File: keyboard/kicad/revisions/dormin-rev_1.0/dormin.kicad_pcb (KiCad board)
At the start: 2 copper layers, 141.5 x 103.1 mm, 108 parts, among them J1 Conn_01x06, J2 Conn_01x04, J3 Conn_01x05, Q1 HX2302A, SW1 SW_Push, SW10 SW_Push, SW11 SW_Push, SW12 SW_Push, SW13 SW_Push, SW14 SW_Push, SW15 SW_Push, SW16 SW_Push, SW17 SW_Push, SW18 SW_Push, SW19 SW_Push, SW2 SW_Push, SW20 SW_Push, SW3 SW_Push, SW4 SW_Push, SW5 SW_Push, SW6 SW_Push, SW7 SW_Push, SW8 SW_Push, SW9 SW_Push, U3 XIAO-nRF52840-Plus-SMD, U4 TPD2E2U06DCK

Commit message: feat: improve schematics and pcb components placements
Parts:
- added C3: 10uF, Capacitor_SMD:C_0603_1608Metric, B.Cu at (74.1, 96.2)
- added C4: 100nF, Capacitor_SMD:C_0603_1608Metric, B.Cu at (68.4, 96.1)
- added Q2: AO3407A, Package_TO_SOT_SMD:SOT-23, B.Cu at (199.9, 124.0)
- added R710: 100R, Resistor_SMD:R_0603_1608Metric, B.Cu at (199.7, 119.4)
- added R711: 100k, Resistor_SMD:R_0603_1608Metric, B.Cu at (201.4, 119.4)
- added R712: 330R, Resistor_SMD:R_0603_1608Metric, B.Cu at (197.9, 119.4)
- D27: footprint Diode_SMD:Nexperia_CFP3_SOD-123W -> Diode_SMD:D_SOD-523
- D28: value SMF5V0A -> KPESD5V0S1UL; footprint Diode_SMD:D_SMF -> Diode_SMD:D_SOD-882
- J3: value Conn_01x05 -> Conn_01x04
- JST1: footprint willkeebs_power:JST_1.25mm -> Connector_JST:JST_GH_SM02B-GHS-TB_1x02-1MP_P1.25mm_Horizontal
- PSW1: footprint willkeebs_power:Switch_MSK12C02 -> PCM_marbastlib-various:SW_MSK12C02-HB
- Q1: value HX2302A -> AO3400A
- R23, R5, R6: footprint Resistor_SMD:R_0402_1005Metric -> Resistor_SMD:R_0603_1608Metric
- RSW1: footprint willkeebs_components:SW_Push_1P1T_XKB_TS-1187A -> Button_Switch_SMD:SW_SPST_SKQG_WithStem
- moved C2 20.5 mm to (181.2, 103.7), turned to 90 degrees
- moved C1 20.5 mm to (179.4, 103.7), turned to 90 degrees
- moved F2 18.6 mm to (197.5, 133.4), turned to 0 degrees
- moved D27 15.5 mm to (198.5, 131.3), turned to 0 degrees
- moved R1 15.3 mm to (164.2, 103.7), turned to 90 degrees
- moved R6 13.5 mm to (186.1, 119.4)
- moved R5 13.2 mm to (187.9, 119.4)
- moved R23 13.0 mm to (189.6, 119.4)
- moved D11 4.92 mm to (68.5, 114.1), turned to -90 degrees
- moved R706 3.70 mm to (188.9, 128.8)
- moved Q1 3.70 mm to (185.4, 131.0)
- moved R707 3.70 mm to (188.9, 133.3)
- moved D28 1.74 mm to (198.8, 129.6), turned to 0 degrees
- moved U4 0.57 mm to (198.1, 136.1)
- turned D14 to 180 degrees
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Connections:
- net LED_SWITCH renamed BL_DRAIN
- D21 pad 2: RGB_DATA -> Net-(D21-DIN)
- D21 pad 3: 3V3 -> EXT_VCC
- D22 pad 3: 3V3 -> EXT_VCC
- D23 pad 3: 3V3 -> EXT_VCC
- D24 pad 3: 3V3 -> EXT_VCC
- U3 pad 17: RGB_DATA -> STS_LED_DATA
- U3 pad 19: unconnected-(U3-D15_NFC2-Pad19) -> POWER_PIN
- U3 pad 21: EXTB -> EXTA
- U3 pad 22: EXTA -> EXTB
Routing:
- net 5V: track 0.00 -> 40.2 mm
- net VBAT: track 0.00 -> 26.7 mm
- net EXT_VCC: track 0.00 -> 23.2 mm
- net Net-(D22-DOUT): track 0.00 -> 17.2 mm, vias 0 -> 2
- net Net-(D23-DOUT): track 0.00 -> 15.8 mm, vias 0 -> 2
- net Net-(D21-DOUT): track 0.00 -> 15.7 mm
- net GND: track 0.00 -> 11.1 mm, vias 0 -> 4
- net Net-(J3-Pin_3): track 0.00 -> 9.55 mm, vias 0 -> 2
- net Net-(J3-Pin_4): track 0.00 -> 9.44 mm, vias 0 -> 2
- net Net-(D27-K): track 0.00 -> 9.11 mm
- net Net-(D27-A): track 0.00 -> 2.24 mm

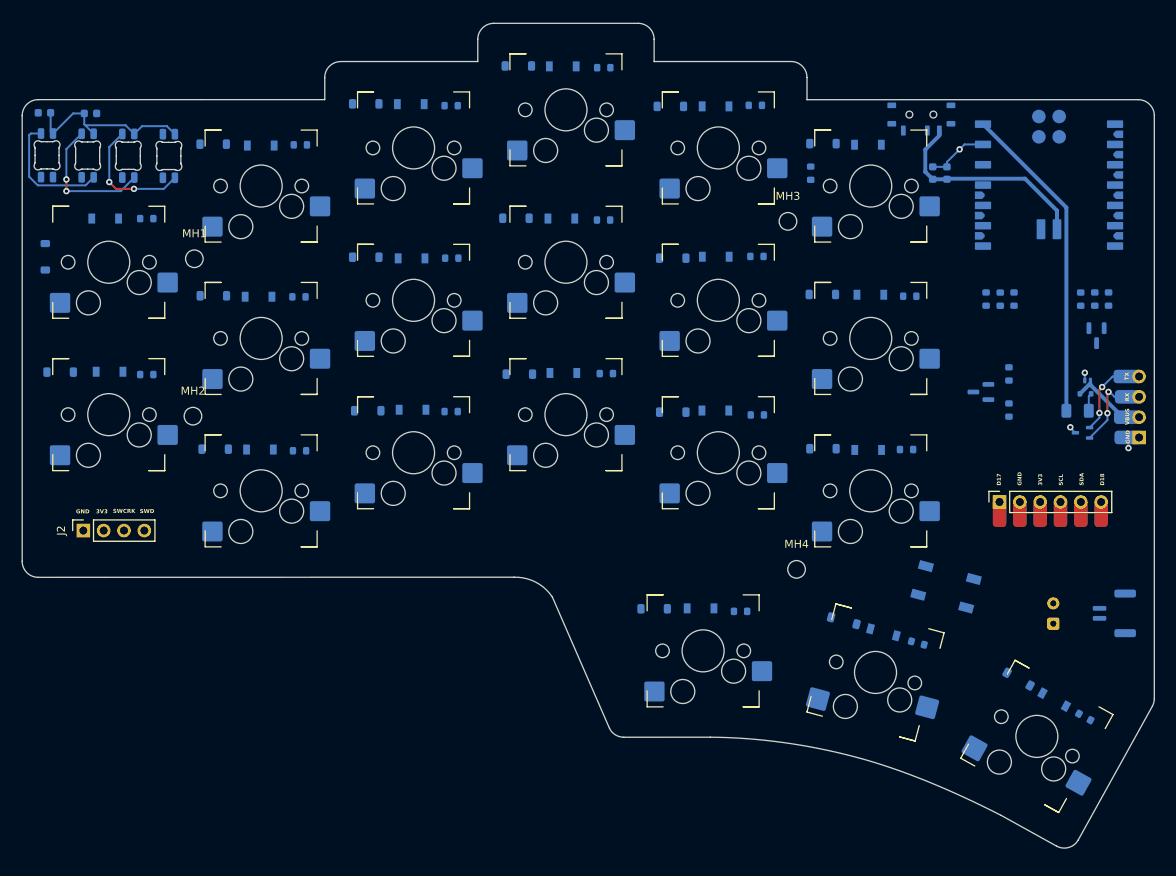
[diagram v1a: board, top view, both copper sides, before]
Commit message: feat: improve schematics and components placement
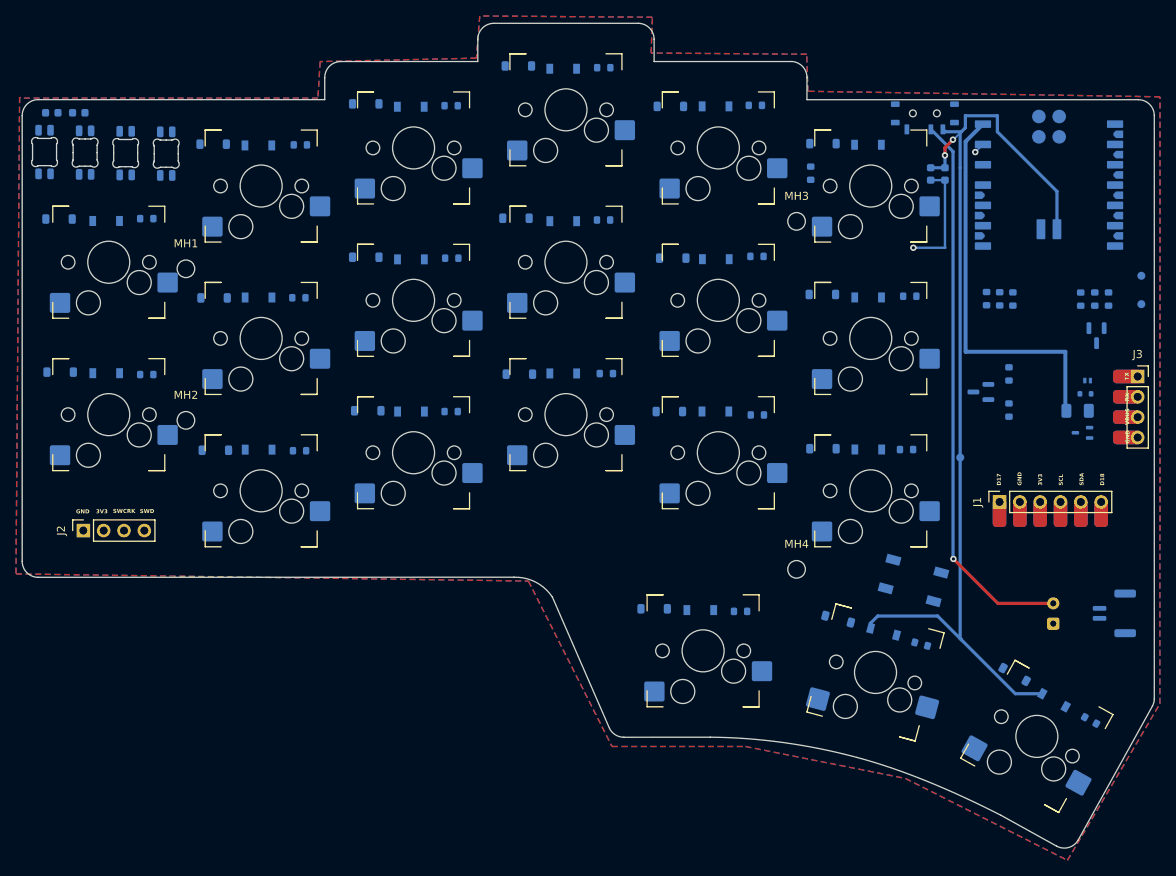
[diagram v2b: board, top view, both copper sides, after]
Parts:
- added TP1: VBAT, TestPoint:TestPoint_Pad_D1.0mm, B.Cu at (182.9, 139.2)
- added TP2: GND, TestPoint:TestPoint_Pad_D1.0mm, B.Cu at (205.5, 120.0)
- added TP3: STS_LED_EN, TestPoint:TestPoint_Pad_D1.0mm, B.Cu at (205.5, 116.5)
- J3: moved to F.Cu
- moved J3 7.62 mm to (205.0, 129.1)
- moved D11 5.02 mm to (70.2, 109.4), turned to 180 degrees
- moved RSW1 4.15 mm to (177.0, 154.6)
- moved R23 1.79 mm to (187.8, 119.4)
- moved MH1 1.64 mm to (86.1, 115.6)
- moved R5 1.58 mm to (189.4, 119.4)
- moved C3 1.47 mm to (72.7, 96.1)
- moved MH3 1.08 mm to (162.4, 109.7)
- moved MH2 1.02 mm to (86.1, 134.6)
- moved C4 0.92 mm to (69.3, 96.1)
- moved R22 0.84 mm to (199.2, 172.1)
- moved D18 0.77 mm to (189.7, 166.3)
- moved D19 0.74 mm to (167.6, 159.4), turned to 165 degrees
- moved D21 0.51 mm to (68.4, 101.0)
- moved D22 0.49 mm to (73.5, 101.1)
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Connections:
- net EXT_VCC renamed Net-(D21-VDD)
- net POWER_PIN renamed STS_LED_EN
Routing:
- net VBAT: track 26.7 -> 123.0 mm, vias 0 -> 2
- net VBAT_RAW: track 0.00 -> 69.6 mm, vias 0 -> 1
- net Net-(D21-VDD): track 23.2 -> 0.00 mm
- net Net-(D22-DOUT): track 17.2 -> 0.00 mm, vias 2 -> 0
- net Net-(D23-DOUT): track 15.8 -> 0.00 mm, vias 2 -> 0
- net Net-(D21-DOUT): track 15.7 -> 0.00 mm
- net Net-(J3-Pin_3): track 9.55 -> 0.00 mm, vias 2 -> 0
- net Net-(J3-Pin_4): track 9.44 -> 0.00 mm, vias 2 -> 0
- net Net-(D27-K): track 9.11 -> 0.00 mm
- net 5V: track 40.2 -> 49.3 mm
- net GND: track 11.1 -> 15.6 mm, vias 4 -> 2
- net Net-(D27-A): track 2.24 -> 0.00 mm
- added copper zone on B.Cu, net (none)
- added copper zone on F.Cu, net (none)
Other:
- board text added: "VBAT"

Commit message: chore: added panelized boards
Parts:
- removed BT1: Pads, willkeebs_power:Battery_Pad
- removed C1, C3: 10uF, Capacitor_SMD:C_0603_1608Metric
- removed C2, C4: 100nF, Capacitor_SMD:C_0603_1608Metric
- removed D1, D10, D11, D12, D13, D14, D15, D16, D17, D18, D19, D2, D20, D3, D4, D5, D6, D7, D8, D9: 1N4148W, Diode_SMD:D_SOD-123
- removed D21, D22, D23, D24: SK6812MINI-E, LED_SMD:LED_SK6812MINI-E_3.2x2.8mm_P1.5mm_ReverseMount
- removed D25, D26, D29, D30, D31, D32, D33, D34, D35, D36, D37, D38, D39, D40, D41, D42, D43, D44, D45, D46: LED, willkeebs_components:LED_MHT151WDT
- removed D27: D_Schottky, Diode_SMD:D_SOD-523
- removed D28: KPESD5V0S1UL, Diode_SMD:D_SOD-882
- removed F2: Polyfuse, Fuse:Fuse_1206_3216Metric
- removed J1: Conn_01x06, willkeebs_misc:SMD_Conn_1x06_P2.54mm_Vertical
- removed J2: Conn_01x04, Connector_PinSocket_2.54mm:PinSocket_1x04_P2.54mm_Vertical
- removed J3: Conn_01x04, willkeebs_misc:SMD_Conn_1x04_P2.54mm_Vertical
- removed JST1: Conn_01x02_Pin, Connector_JST:JST_GH_SM02B-GHS-TB_1x02-1MP_P1.25mm_Horizontal
- removed MH1, MH2, MH3, MH4: MountingHole_2.2mm_M2, MountingHole:MountingHole_2.2mm_M2
- removed PSW1: SW_SPDT, PCM_marbastlib-various:SW_MSK12C02-HB
- removed Q1: AO3400A, Package_TO_SOT_SMD:SOT-23
- removed Q2: AO3407A, Package_TO_SOT_SMD:SOT-23
- removed R1, R10, R11, R12, R13, R14, R15, R16, R17, R18, R19, R2, R20, R21, R22, R3, R4, R7, R8, R9: 1K, Resistor_SMD:R_0603_1608Metric
- removed R23, R706, R710: 100R, Resistor_SMD:R_0603_1608Metric
- removed R5, R6: 33R, Resistor_SMD:R_0603_1608Metric
- removed R707: 10k, Resistor_SMD:R_0603_1608Metric
- removed R711: 100k, Resistor_SMD:R_0603_1608Metric
- removed R712: 330R, Resistor_SMD:R_0603_1608Metric
- removed RSW1: RSW1, Button_Switch_SMD:SW_SPST_SKQG_WithStem
- removed TP1: VBAT, TestPoint:TestPoint_Pad_D1.0mm
- removed TP2: GND, TestPoint:TestPoint_Pad_D1.0mm
- removed TP3: STS_LED_EN, TestPoint:TestPoint_Pad_D1.0mm
- removed U3: XIAO-nRF52840-Plus-SMD, Seeed_Studio_XIAO_Series:XIAO-nRF52840-Plus-SMD
- removed U4: TPD2E2U06DCK, Package_TO_SOT_SMD:SOT-323_SC-70
- added SW21: SW_Push, SW_MX_Choc_Hotswap, F.Cu at (344.4, 134.0)
- added SW22: SW_Push, SW_MX_Choc_Hotswap, F.Cu at (344.4, 115.0)
- added SW23: SW_Push, SW_MX_Choc_Hotswap, F.Cu at (325.3, 143.6)
- added SW24: SW_Push, SW_MX_Choc_Hotswap, F.Cu at (325.3, 124.5)
- added SW25: SW_Push, SW_MX_Choc_Hotswap, F.Cu at (325.3, 105.5)
- added SW26: SW_Push, SW_MX_Choc_Hotswap, F.Cu at (306.3, 138.8)
- added SW27: SW_Push, SW_MX_Choc_Hotswap, F.Cu at (306.3, 119.7)
- added SW28: SW_Push, SW_MX_Choc_Hotswap, F.Cu at (306.3, 100.7)
- added SW29: SW_Push, SW_MX_Choc_Hotswap, F.Cu at (287.2, 134.0)
- added SW30: SW_Push, SW_MX_Choc_Hotswap, F.Cu at (287.2, 115.0)
- added SW31: SW_Push, SW_MX_Choc_Hotswap, F.Cu at (287.2, 95.9)
- added SW32: SW_Push, SW_MX_Choc_Hotswap, F.Cu at (268.2, 138.8)
- added SW33: SW_Push, SW_MX_Choc_Hotswap, F.Cu at (268.2, 119.7)
- added SW34: SW_Push, SW_MX_Choc_Hotswap, F.Cu at (268.2, 100.7)
- added SW35: SW_Push, SW_MX_Choc_Hotswap, F.Cu at (249.1, 143.6)
- added SW36: SW_Push, SW_MX_Choc_Hotswap, F.Cu at (249.1, 124.5)
- added SW37: SW_Push, SW_MX_Choc_Hotswap, F.Cu at (249.1, 105.5)
- added SW38: SW_Push, SW_MX_Choc_Hotswap, F.Cu at (270.1, 163.6)
- added SW39: SW_Push, SW_MX_Choc_Hotswap, F.Cu at (248.5, 166.3)
- added SW40: SW_Push, SW_MX_Choc_Hotswap, F.Cu at (228.4, 174.3)
- SW1, SW10, SW11, SW12, SW13, SW14, SW15, SW16, SW17, SW18, SW19, SW2, SW20, SW3, SW4, SW5, SW6, SW7, SW8, SW9: footprint willkeebs_keyboard:NF_LED_1206_SW_KS33_3_0_HS_1U -> SW_MX_Choc_Hotswap
- moved SW1 99.6 mm to (76.3, 134.0), turned to 0 degrees
- moved SW17 99.2 mm to (171.5, 105.5), turned to 0 degrees
- moved SW16 78.3 mm to (171.5, 124.5), turned to 0 degrees
- moved SW2 77.7 mm to (76.3, 115.0), turned to 0 degrees
- moved SW3 61.2 mm to (95.3, 143.6), turned to 0 degrees
- moved SW11 60.0 mm to (133.4, 95.9), turned to 0 degrees
- moved SW6 59.1 mm to (114.4, 138.8), turned to 0 degrees
- moved SW15 57.2 mm to (171.5, 143.6), turned to 0 degrees
- moved SW18 43.2 mm to (150.6, 163.6), turned to 0 degrees
- moved SW20 43.0 mm to (192.3, 174.3), turned to -29 degrees
- moved SW10 39.1 mm to (133.4, 115.0), turned to 0 degrees
- moved SW7 38.3 mm to (114.4, 119.7), turned to 0 degrees
- moved SW14 38.2 mm to (152.5, 100.7), turned to 0 degrees
- moved SW4 30.7 mm to (95.3, 124.5), turned to 0 degrees
- moved SW8 23.8 mm to (114.4, 100.7), turned to 0 degrees
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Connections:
- SW1 pad 1: Net-(D1-A) -> outer_home_from
- SW1 pad 2: COL5 -> outer_home_to
- SW10 pad 1: Net-(D10-A) -> middle_home_from
- SW10 pad 2: COL1 -> middle_home_to
- SW11 pad 1: Net-(D11-A) -> middle_top_from
- SW11 pad 2: COL0 -> middle_top_to
- SW12 pad 1: Net-(D12-A) -> index_bottom_from
- SW12 pad 2: COL5 -> index_bottom_to
- SW13 pad 1: Net-(D13-A) -> index_home_from
- SW13 pad 2: COL4 -> index_home_to
- SW14 pad 1: Net-(D14-A) -> index_top_from
- SW14 pad 2: COL3 -> index_top_to
- SW15 pad 1: Net-(D15-A) -> inner_bottom_from
- SW15 pad 2: COL2 -> inner_bottom_to
- SW16 pad 1: Net-(D16-A) -> inner_home_from
- SW16 pad 2: COL1 -> inner_home_to
- SW17 pad 1: Net-(D17-A) -> inner_top_from
- SW17 pad 2: COL0 -> inner_top_to
- SW18 pad 1: Net-(D18-A) -> inner_only_from
- SW18 pad 2: COL5 -> inner_only_to
- SW19 pad 1: Net-(D19-A) -> home_only_from
- SW19 pad 2: COL4 -> home_only_to
- SW2 pad 1: Net-(D2-A) -> outer_top_from
- SW2 pad 2: COL4 -> outer_top_to
- SW20 pad 1: Net-(D20-A) -> outer_only_from
- SW20 pad 2: COL3 -> outer_only_to
- SW3 pad 1: Net-(D3-A) -> pinky_bottom_from
- SW3 pad 2: COL3 -> pinky_bottom_to
- SW4 pad 1: Net-(D4-A) -> pinky_home_from
- SW4 pad 2: COL2 -> pinky_home_to
- SW5 pad 1: Net-(D5-A) -> pinky_top_from
- SW5 pad 2: COL1 -> pinky_top_to
- SW6 pad 1: Net-(D6-A) -> ring_bottom_from
- SW6 pad 2: COL5 -> ring_bottom_to
- SW7 pad 1: Net-(D7-A) -> ring_home_from
- SW7 pad 2: COL4 -> ring_home_to
- SW8 pad 1: Net-(D8-A) -> ring_top_from
- SW8 pad 2: COL3 -> ring_top_to
- SW9 pad 1: Net-(D9-A) -> middle_bottom_from
- SW9 pad 2: COL2 -> middle_bottom_to
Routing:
- net VBAT: track 123.0 -> 0.00 mm, vias 2 -> 0
- net VBAT_RAW: track 69.6 -> 0.00 mm, vias 1 -> 0
- net 5V: track 49.3 -> 0.00 mm
- net GND: track 15.6 -> 0.00 mm, vias 2 -> 0
- removed copper zone on B.Cu, net (none)
- removed copper zone on F.Cu, net (none)
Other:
- board size 141.5 x 103.1 mm -> 290.1 x 103.4 mm
- board text removed: "3V3"
- board text removed: "D17"
- board text removed: "D18"
- board text removed: "GND"
- board text removed: "RX"
- board text removed: "SCL"
- board text removed: "SDA"
- board text removed: "SWCRK"
- board text removed: "SWD"
- board text removed: "TX"
- board text removed: "VBAT"
- board text removed: "VBUS"
